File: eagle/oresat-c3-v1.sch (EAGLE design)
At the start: 166 parts, among them J1 J-SAMTEC-TFM-110-X1-XXX-D-RA, J10 U.FL, J11 U.FL, J13 U.FL, J14 U.FL, J15 HARWIN-2X8X1.27, J19 HARWIN-2X8X1.27, J2 U.FL, J3 U.FL, J4 U.FL, J6 J-SAMTEC-TFM-120-X1-XXX-D-RA, J7 FTSH-105-XX-X-DV-K, J8 U.FL, J9 U.FL, Q1 MOSFET-PCH-SOT23-6, U1 MAX892LEUA+T21-0036K-L, U11 U-ONSEMI-AX5043, U12 LP2985XX-N, U13 U-ONSEMI-AX5043, U14 LP2985XX-N, U2 TCAN330, U3 TCAN330, U4 TPS259621 - eFuse, U5 TPS62111RSA, U6 MAX6374KA-T21-0078H-L, U7 STM32F446RE, U9 SFEM016GB1EM1TO-A-HG-111-STD, X1 16MHZ-2.5x2mm, X3 TAITIEN-TY, X4 TAITIEN-TY

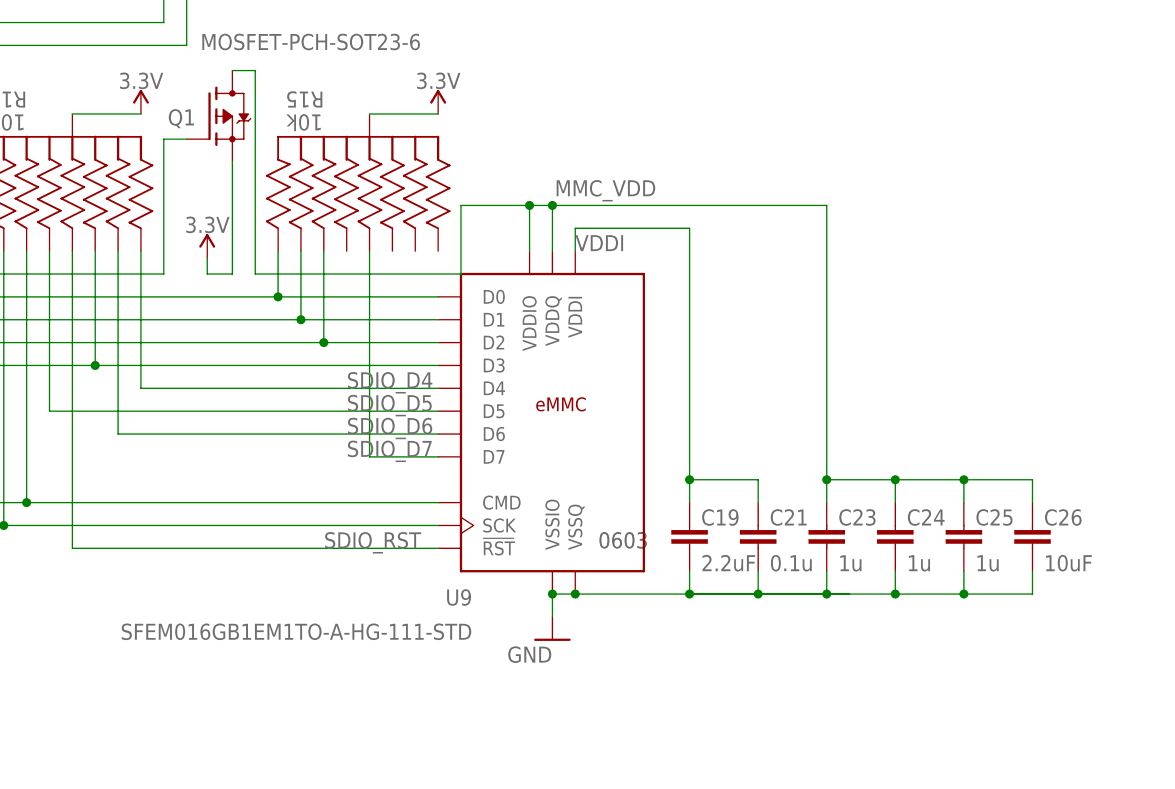
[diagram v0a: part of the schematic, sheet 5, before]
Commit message: Cleared all ERC and DRC
Made design changes as per design review
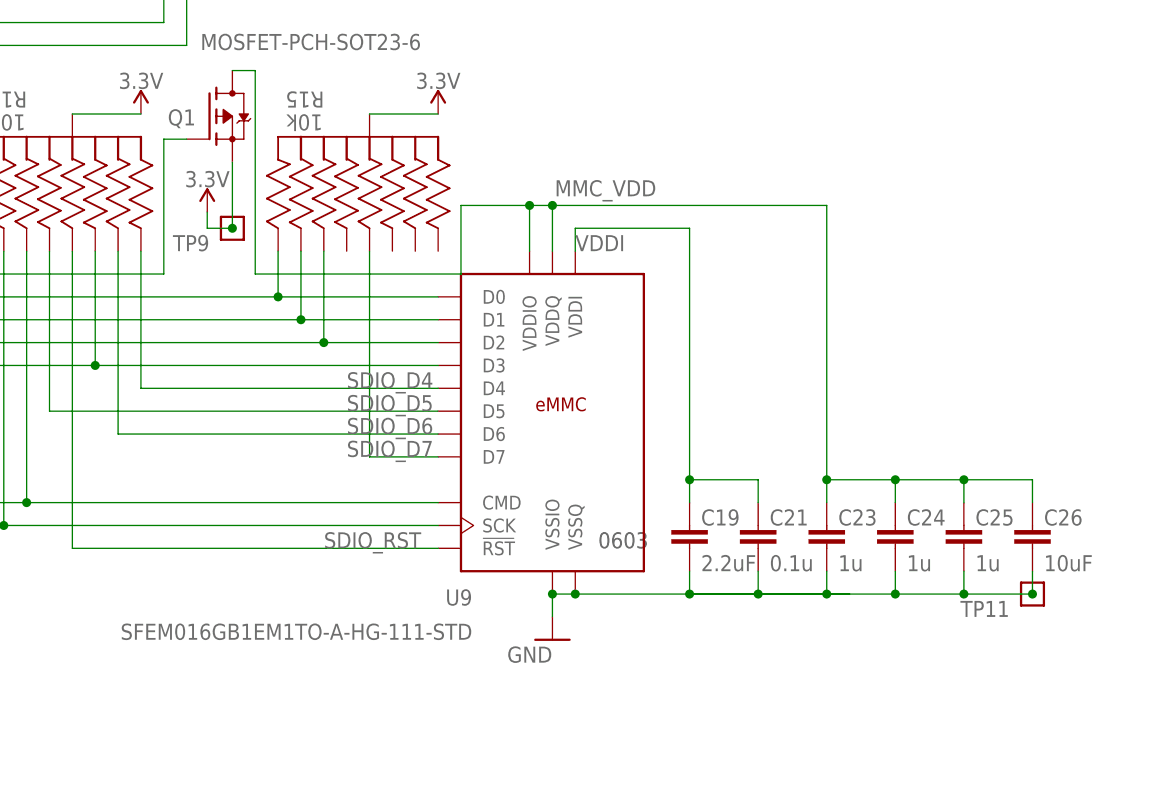
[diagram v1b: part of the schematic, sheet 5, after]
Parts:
- added TP11, TP9: TEST-POINT, Tova:TEST-POINT
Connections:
- net 3.3V: now also TP9.1
- net GND: now also TP11.1
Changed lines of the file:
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@@
 <part name="GND56" library="supply1" library_urn="urn:adsk.eagle:library:371" deviceset="GND" device=""/>
 <part name="GND57" library="supply1" library_urn="urn:adsk.eagle:library:371" deviceset="GND" device=""/>
+<part name="TP9" library="Tova" deviceset="TEST-POINT" device=""/>
+<part name="TP11" library="Tova" deviceset="TEST-POINT" device=""/>
 </parts>
 <sheets>
@@
 <attribute name="VALUE" x="347.98" y="101.854" size="1.778" layer="96" rot="MR0" align="bottom-center"/>
 </instance>
-<instance part="SUPPLY18" gate="G$1" x="322.326" y="83.058" smashed="yes" rot="MR0">
-<attribute name="VALUE" x="322.326" y="85.852" size="1.778" layer="96" rot="MR0" align="bottom-center"/>
+<instance part="SUPPLY18" gate="G$1" x="322.326" y="88.138" smashed="yes" rot="MR0">
+<attribute name="VALUE" x="322.326" y="90.932" size="1.778" layer="96" rot="MR0" align="bottom-center"/>
 </instance>
 <instance part="GND35" gate="1" x="360.68" y="40.64" smashed="yes" rot="MR0">
@@
 <attribute name="NAME" x="154.94" y="111.76" size="1.778" layer="95" font="vector"/>
 </instance>
+<instance part="TP9" gate="G$1" x="325.12" y="86.36" smashed="yes" rot="MR0">
+<attribute name="NAME" x="322.58" y="83.82" size="1.778" layer="95" font="vector" rot="MR0"/>
+</instance>
+<instance part="TP11" gate="G$1" x="414.02" y="45.72" smashed="yes" rot="MR0">
+<attribute name="NAME" x="411.48" y="43.18" size="1.778" layer="95" font="vector" rot="MR0"/>
+</instance>
 </instances>
 <busses>
@@
 <junction x="360.68" y="45.72"/>
 <junction x="363.22" y="45.72"/>
+<pinref part="TP11" gate="G$1" pin="1"/>
+<junction x="414.02" y="45.72"/>
 </segment>
 </net>
@@
 <segment>
 <pinref part="Q1" gate="G$1" pin="S"/>
-<wire x1="325.12" y1="93.726" x2="325.12" y2="81.28" width="0.1524" layer="91"/>
+<wire x1="325.12" y1="93.726" x2="325.12" y2="86.36" width="0.1524" layer="91"/>
 <pinref part="SUPPLY18" gate="G$1" pin="3.3V"/>
-<wire x1="325.12" y1="81.28" x2="322.326" y2="81.28" width="0.1524" layer="91"/>
-<wire x1="322.326" y1="81.28" x2="322.326" y2="83.058" width="0.1524" layer="91"/>
+<wire x1="325.12" y1="86.36" x2="322.326" y2="86.36" width="0.1524" layer="91"/>
+<wire x1="322.326" y1="86.36" x2="322.326" y2="88.138" width="0.1524" layer="91"/>
+<pinref part="TP9" gate="G$1" pin="1"/>
+<junction x="325.12" y="86.36"/>
 </segment>
 </net>

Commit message: final stamp, minor schematic clean up and error checking
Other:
- note added: "*Note: Pins 8,11,12,21 left intentionally floating"
- note removed: "*Note: Pins 11,12,21,8 left intentionally floating"
- note removed: "0.1" header"
- note removed: "Radio 1 - 0.05" header 1"
- note removed: "Radio 1 - 0.05" header 2"
- note removed: "Radio 2 - 0.05" header 1"
- note removed: "Radio 2 - 0.05" header 2"
- moved on the sheet: C45, C50, C51, C52, C61, Q1, TP9, X3, X4
